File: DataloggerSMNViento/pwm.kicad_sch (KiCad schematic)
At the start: 4 parts

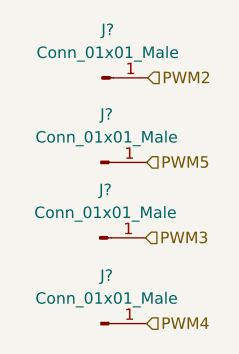
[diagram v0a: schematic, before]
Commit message: Agrego modificaciones al poncho de la EDU CIAA, también agrego una simulacion del circuito para tomar la tensión del ADC del tunnel
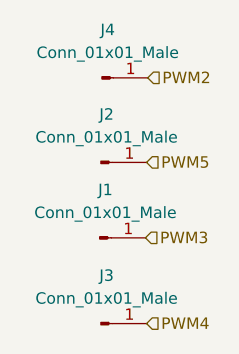
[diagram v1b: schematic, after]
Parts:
- J1, J2, J3, J4: renamed from J?; footprint (none) -> Connector_Pin:Pin_D1.0mm_L10.0mm
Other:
- company: (none) -> Servicio Meteorológico Nacional - FIUBA - UBA
- title: (none) -> Datalogger para SCTV
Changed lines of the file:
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@@
 (kicad_sch (version 20211123) (generator eeschema)
   (paper "A4")
+  (title_block
+    (title "Datalogger para SCTV")
+    (date "2023-10-20")
+    (rev "1.0")
+    (company "Servicio Meteorológico Nacional - FIUBA - UBA")
+    (comment 1 "poner repo")
+    (comment 2 "Autores y Licencia del poncho: Cristian Aranda (FIUBA), ver archivo licence.txt")
+    (comment 3 "Autor del poncho: Cristian Zozimo Aranda Cordero.  Ver directorio \"doc\"")
+    (comment 4 "CÓDIGO PONCHO: DT1")
+  )
   (hierarchical_label "PWM3" (shape input) (at 100.457 59.944 0)
     (effects (font (size 1.27 1.27)) (justify left))
@@
   (symbol (lib_id "Connector:Conn_01x01_Male") (at 95.504 51.562 0) (unit 1)
     (in_bom yes) (on_board yes) (fields_autoplaced)
-    (property "Reference" "J?" (id 0) (at 96.139 46.228 0))
+    (property "Reference" "J2" (id 0) (at 96.139 46.228 0))
     (property "Value" "Conn_01x01_Male" (id 1) (at 96.139 48.768 0))
-    (property "Footprint" "" (id 2) (at 95.504 51.562 0)
+    (property "Footprint" "Connector_Pin:Pin_D1.0mm_L10.0mm" (id 2) (at 95.504 51.562 0)
       (effects (font (size 1.27 1.27)) hide)
     )
@@
   (symbol (lib_id "Connector:Conn_01x01_Male") (at 95.377 59.944 0) (unit 1)
     (in_bom yes) (on_board yes)
-    (property "Reference" "J?" (id 0) (at 96.012 54.61 0))
+    (property "Reference" "J1" (id 0) (at 96.012 54.61 0))
     (property "Value" "Conn_01x01_Male" (id 1) (at 96.012 57.15 0))
-    (property "Footprint" "" (id 2) (at 95.377 59.944 0)
+    (property "Footprint" "Connector_Pin:Pin_D1.0mm_L10.0mm" (id 2) (at 95.377 59.944 0)
       (effects (font (size 1.27 1.27)) hide)
     )
@@
   (symbol (lib_id "Connector:Conn_01x01_Male") (at 95.504 69.469 0) (unit 1)
     (in_bom yes) (on_board yes) (fields_autoplaced)
-    (property "Reference" "J?" (id 0) (at 96.139 64.135 0))
+    (property "Reference" "J3" (id 0) (at 96.139 64.135 0))
     (property "Value" "Conn_01x01_Male" (id 1) (at 96.139 66.675 0))
-    (property "Footprint" "" (id 2) (at 95.504 69.469 0)
+    (property "Footprint" "Connector_Pin:Pin_D1.0mm_L10.0mm" (id 2) (at 95.504 69.469 0)
       (effects (font (size 1.27 1.27)) hide)
     )
@@
   (symbol (lib_id "Connector:Conn_01x01_Male") (at 95.631 42.164 0) (unit 1)
     (in_bom yes) (on_board yes) (fields_autoplaced)
-    (property "Reference" "J?" (id 0) (at 96.266 36.83 0))
+    (property "Reference" "J4" (id 0) (at 96.266 36.83 0))
     (property "Value" "Conn_01x01_Male" (id 1) (at 96.266 39.37 0))
-    (property "Footprint" "" (id 2) (at 95.631 42.164 0)
+    (property "Footprint" "Connector_Pin:Pin_D1.0mm_L10.0mm" (id 2) (at 95.631 42.164 0)
       (effects (font (size 1.27 1.27)) hide)
     )

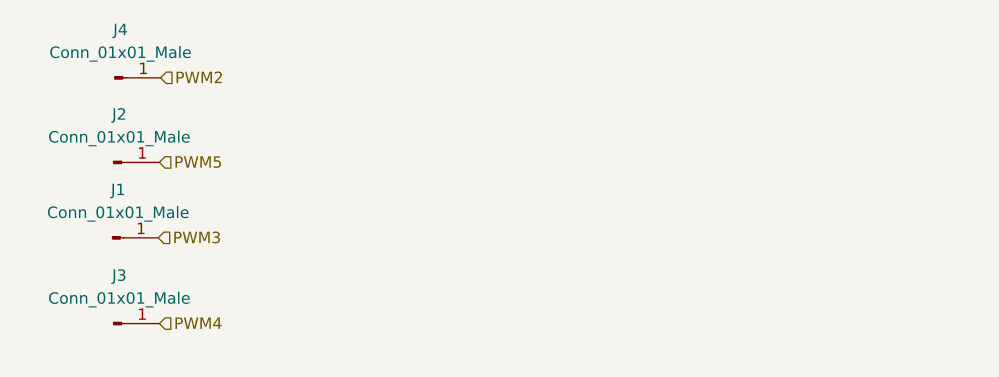
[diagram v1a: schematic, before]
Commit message: Subo la version v1.0 del PCB del poncho de la tesis
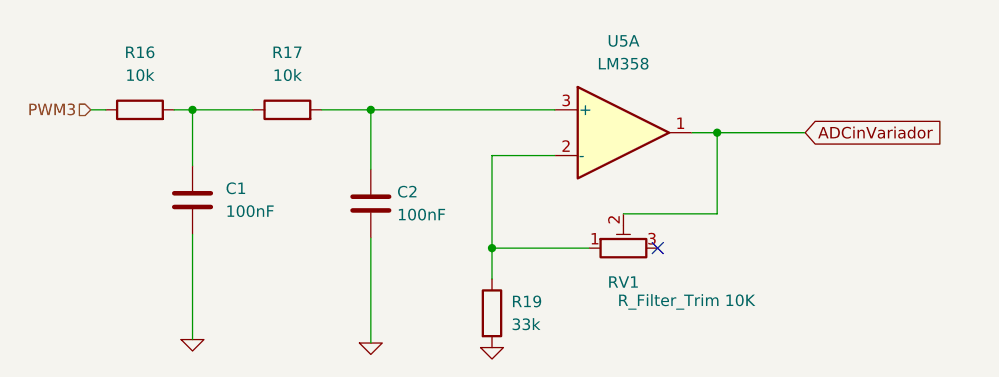
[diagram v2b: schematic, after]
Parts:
- removed J1, J2, J3, J4: Conn_01x01_Male, Connector_Pin:Pin_D1.0mm_L10.0mm, symbol Connector:Conn_01x01_Male
- added C1, C2: 100nF, Capacitor_SMD:C_1206_3216Metric, symbol Device:C
- added R16, R17: 10k, Resistor_SMD:R_1206_3216Metric, symbol Device:R
- added R19: 33k, Resistor_SMD:R_1206_3216Metric, symbol Device:R
- added RV1: R_Filter_Trim 10K, Connector_PinHeader_2.54mm:PinHeader_1x03_P2.54mm_Vertical, symbol Device:R_Potentiometer_Trim
- added U5: LM358, Package_SO:SO-8_3.9x4.9mm_P1.27mm, symbol Amplifier_Operational:LM358
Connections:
- net PWM3: now also R16.1
- new net: C1.1, R16.2, R17.1
- new net: C2.1, R17.2, U5.3 (+)
- new net: R19.1, RV1.1, U5.2 (-)
- new net ADCinVariador: RV1.2, U5.1
- new net GND: C1.2, C2.2, R19.2
- no-connect marks 0 -> 1

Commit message: Se debe cambiar el diseño porque el footprint del  StepDown esta invertido, lo cual va a implicar cambiar algunas pistas
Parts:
- U5: footprint Package_SO:SO-8_3.9x4.9mm_P1.27mm -> Package_SO:SOIC-8_3.9x4.9mm_P1.27mm
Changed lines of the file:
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@@
     (property "Reference" "U5" (id 0) (at 152.146 38.1 0))
     (property "Value" "LM358" (id 1) (at 152.146 40.64 0))
-    (property "Footprint" "Package_SO:SO-8_3.9x4.9mm_P1.27mm" (id 2) (at 152.146 48.26 0)
+    (property "Footprint" "Package_SO:SOIC-8_3.9x4.9mm_P1.27mm" (id 2) (at 152.146 48.26 0)
       (effects (font (size 1.27 1.27)) hide)
     )
